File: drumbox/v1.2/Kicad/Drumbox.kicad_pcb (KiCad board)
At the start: 2 copper layers, 286 x 128 mm, 129 parts, among them J1 Power Input, J10 Main OUT, J11 Conn_01x04_Female, J12 Conn_01x04_Male, J13 Conn_01x03_Female, J14 Conn_01x03_Male, J15 Conn_01x04_Female, J16 Conn_01x04_Male, J2 Conn_01x04_Male, J3 Conn_01x04_Male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

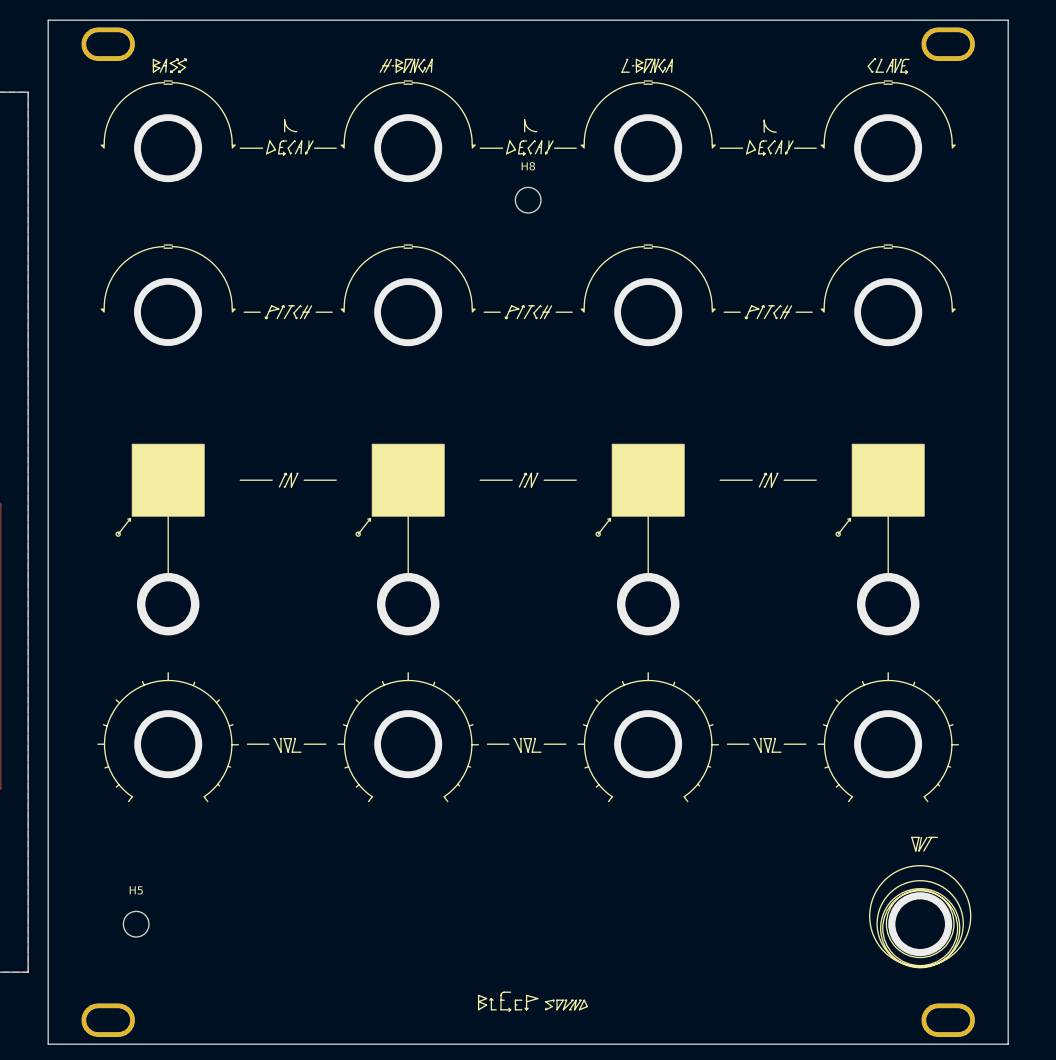
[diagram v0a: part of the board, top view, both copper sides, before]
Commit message: fixed size issues on front panel drumbox
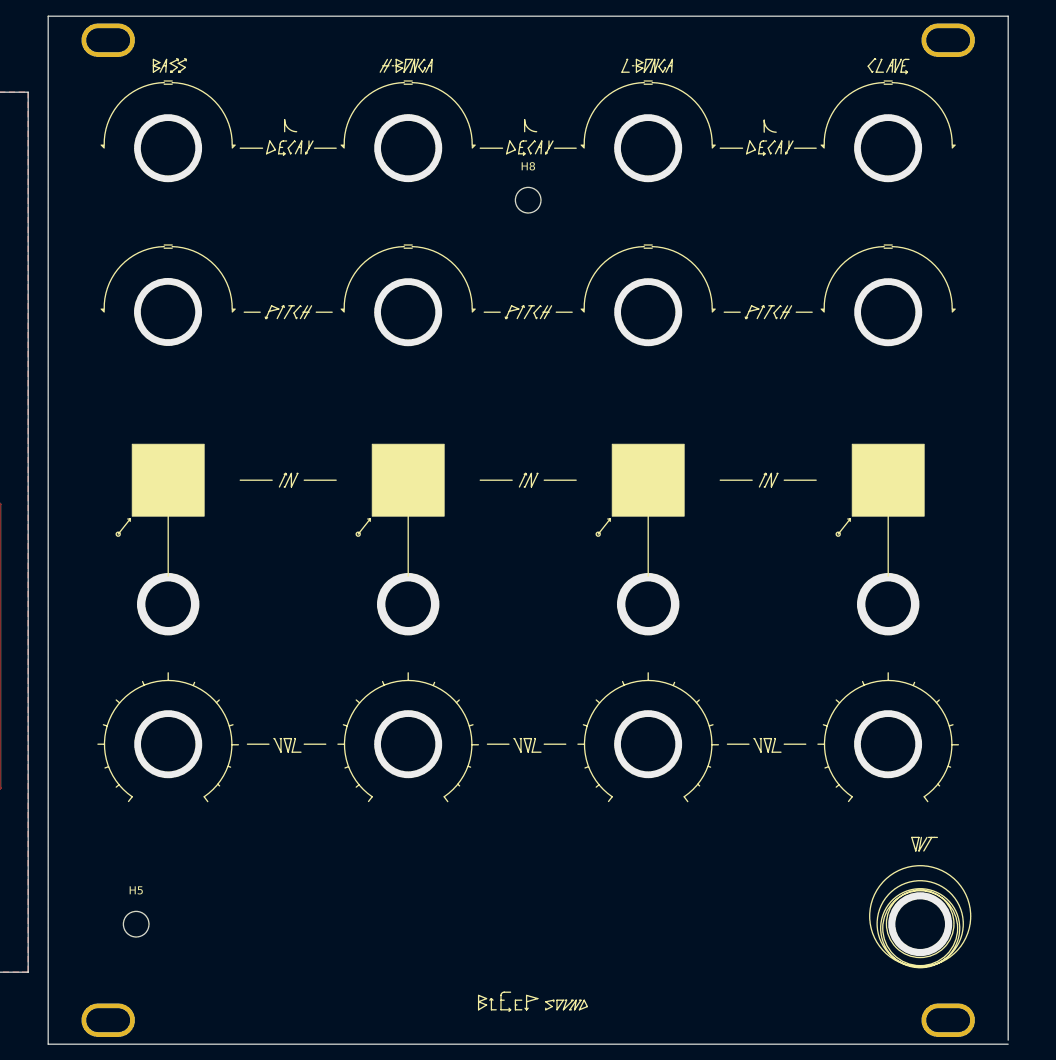
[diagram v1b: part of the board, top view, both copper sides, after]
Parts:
- moved H1 0.50 mm to (203.5, 24.5)
- moved H2 0.50 mm to (308.5, 24.5)
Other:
- board size 286 x 128 mm -> 286 x 128.5 mm
- board text removed: "Drumbox V1.1 BleepSound 2022"
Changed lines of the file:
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@@
   )
   (footprint "Synth:Doepfer Mounting hole" (layer "F.Cu")
-    (at 203.5 25)
+    (at 203.5 24.5)
     (property "Sheetfile" "Socket.kicad_sch")
     (property "Sheetname" "Socket")
@@
   )
   (footprint "Synth:Doepfer Mounting hole" (layer "F.Cu")
-    (at 308.5 25)
+    (at 308.5 24.5)
     (property "Sheetfile" "Socket.kicad_sch")
     (property "Sheetname" "Socket")
@@
   (gr_line (start 73.5 141) (end 193.500001 141) (layer "Edge.Cuts") (width 0.05))
   (gr_line (start 30 31) (end 30 141) (layer "Edge.Cuts") (width 0.05))
-  (gr_line (start 196 22) (end 196 150) (layer "Edge.Cuts") (width 0.05))
-  (gr_line (start 196 22) (end 316 22) (layer "Edge.Cuts") (width 0.05))
-  (gr_line (start 316 22) (end 316 150) (layer "Edge.Cuts") (width 0.05))
+  (gr_line (start 196 21.5) (end 196 150) (layer "Edge.Cuts") (width 0.05))
+  (gr_line (start 196 21.5) (end 316 21.5) (layer "Edge.Cuts") (width 0.05))
+  (gr_line (start 316 21.5) (end 316 149.5) (layer "Edge.Cuts") (width 0.05))
   (gr_line (start 316 150) (end 196 150) (layer "Edge.Cuts") (width 0.05))
   (gr_line (start 30 31) (end 69.999999 31) (layer "Edge.Cuts") (width 0.05))
@@
     (effects (font (size 1 1) (thickness 0.15)) (justify mirror))
   )
-  (gr_text "Drumbox\nV1.1 BleepSound\n2022" (at 257 26.6) (layer "B.SilkS")
+  (gr_text "Drumbox\nV1.2 BleepSound\n2022" (at 257 26.6) (layer "B.SilkS")
     (effects (font (size 1 1) (thickness 0.15)) (justify mirror))
   )
@@
       (effects (font (size 1 1) (thickness 0.15)))
     )
-    (format (units 3) (units_format 1) (precision 4))
-    (style (thickness 0.1) (arrow_length 1.27) (text_position_mode 0) (extension_height 0.58642) (extension_offset 0.5) keep_text_aligned)
-  )
-  (dimension (type aligned) (layer "Dwgs.User")
-    (pts (xy 290 22.5) (xy 316 22.5))
-    (height -2)
-    (gr_text "26,0000 mm" (at 303 19.35) (layer "Dwgs.User")
-      (effects (font (size 1 1) (thickness 0.15)))
-    )
